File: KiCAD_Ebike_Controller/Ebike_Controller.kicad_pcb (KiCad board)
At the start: 4 copper layers, 100 x 100 mm, 118 parts, among them J1 IO, J10 I2C_SCL, J11 I2C_SDA, J2 Prog, J3 Hall Effect Sensors, J4 PHASE_A, J5 PHASE_B, J6 PHASE_C, J7 Micro_SD_Card, J8 +48V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

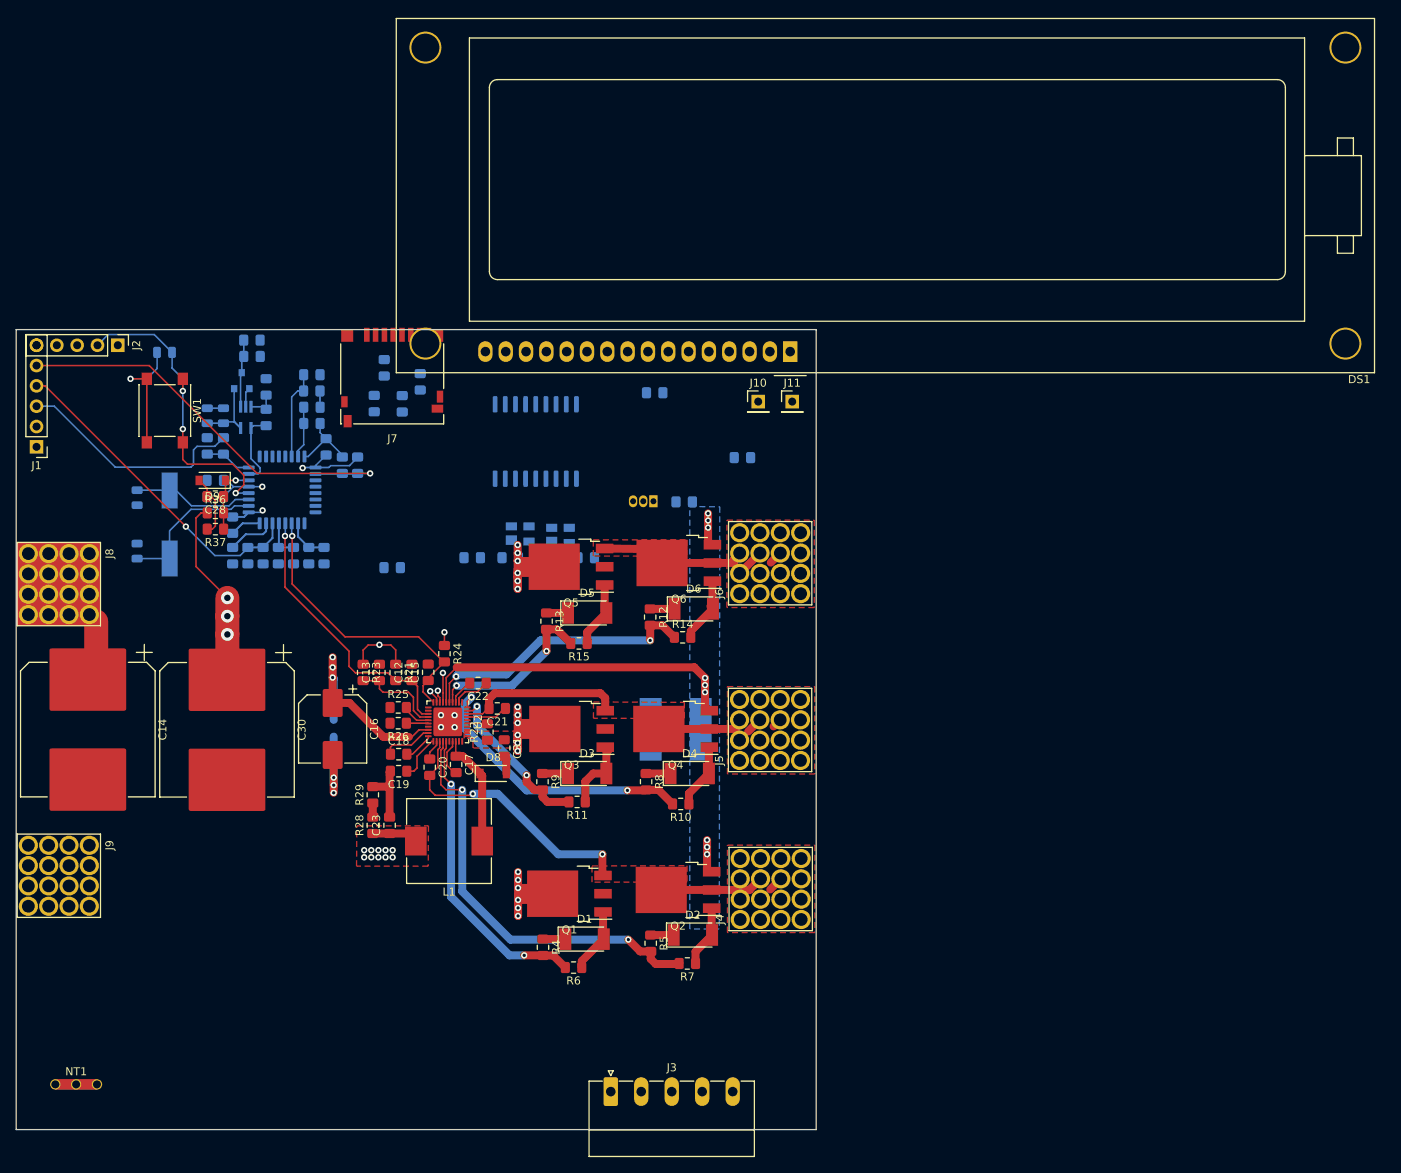
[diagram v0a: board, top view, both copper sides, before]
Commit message: Layout done. will tidy up ref des next
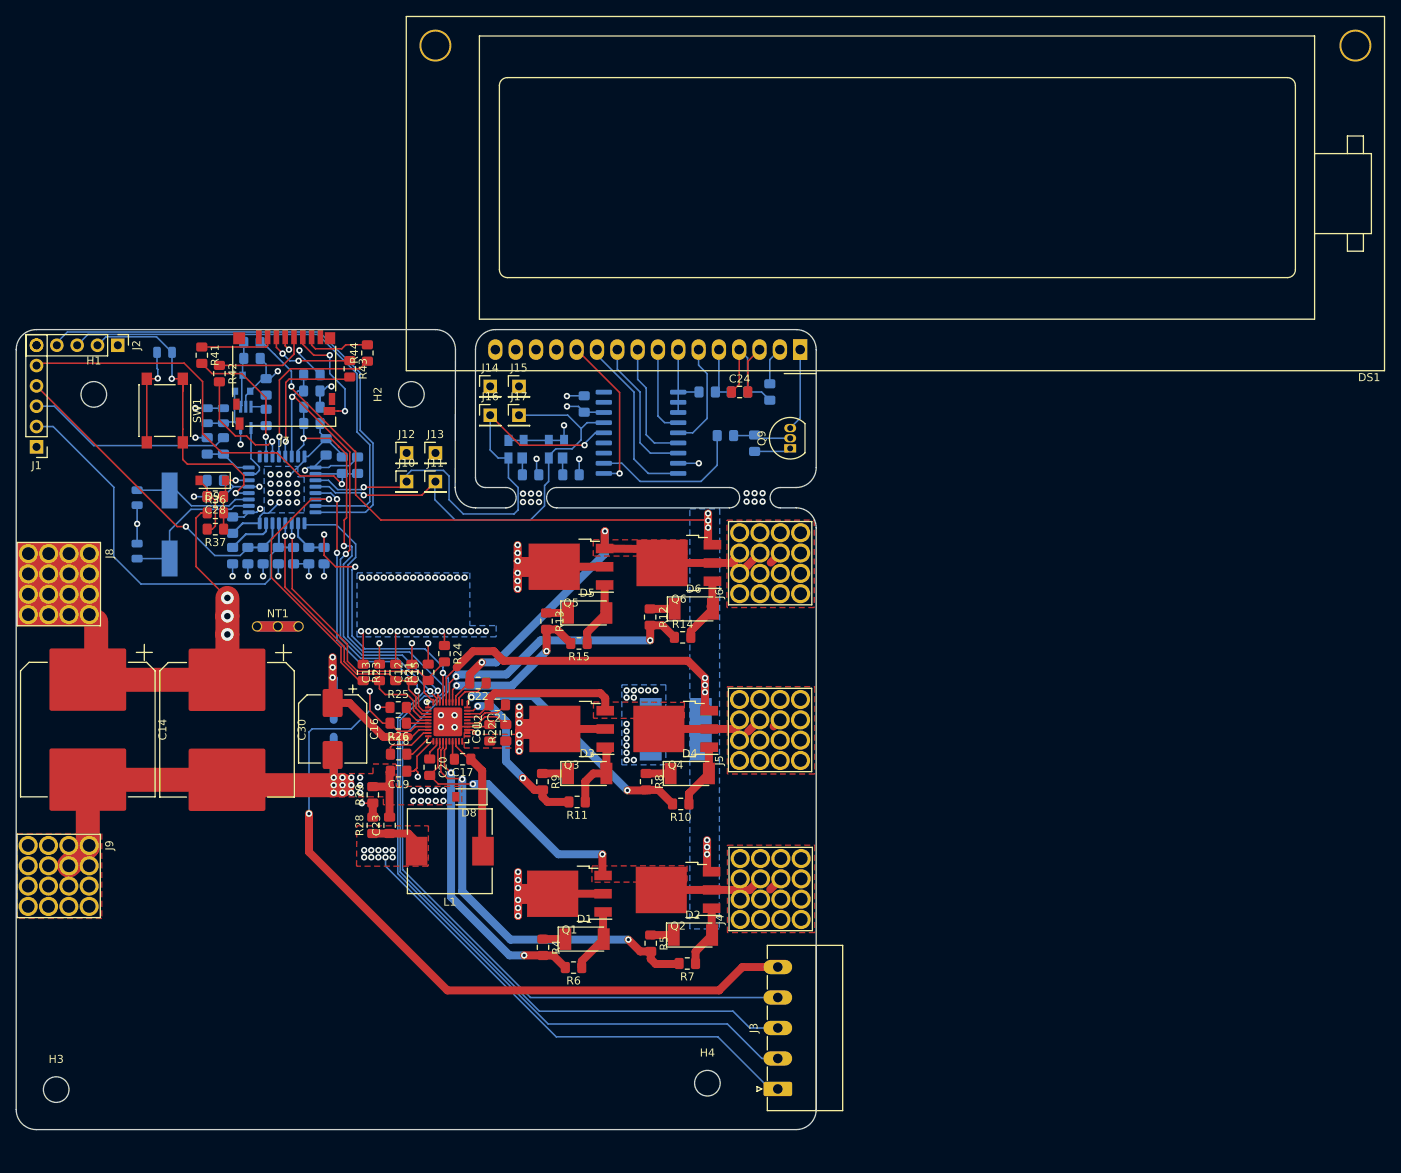
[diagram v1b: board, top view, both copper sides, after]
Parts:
- added H1: MountingHole, MountingHole:MountingHole_3.2mm_M3, F.Cu at (57.7, 67.1)
- added H2: MountingHole, MountingHole:MountingHole_3.2mm_M3, F.Cu at (97.4, 67.1)
- added H3: MountingHole, MountingHole:MountingHole_3.2mm_M3_DIN965, F.Cu at (53.0, 154.0)
- added H4: MountingHole, MountingHole:MountingHole_3.2mm_M3_DIN965, F.Cu at (134.4, 153.2)
- added J12: +3V3, Connector_PinHeader_2.54mm:PinHeader_1x01_P2.54mm_Vertical, F.Cu at (96.8, 74.4)
- added J13: GNDD, Connector_PinHeader_2.54mm:PinHeader_1x01_P2.54mm_Vertical, F.Cu at (100.4, 74.4)
- added J14: +3V3_S, Connector_PinHeader_2.54mm:PinHeader_1x01_P2.54mm_Vertical, F.Cu at (107.2, 66.1)
- added J15: GNDD_S, Connector_PinHeader_2.54mm:PinHeader_1x01_P2.54mm_Vertical, F.Cu at (110.8, 66.1)
- added J16: I2C_SCL_S, Connector_PinHeader_2.54mm:PinHeader_1x01_P2.54mm_Vertical, F.Cu at (107.2, 69.7)
- added J17: I2C_SDA_S, Connector_PinHeader_2.54mm:PinHeader_1x01_P2.54mm_Vertical, F.Cu at (110.8, 69.7)
- C24, Q9, R41, R42, R43, R44: moved to F.Cu
- moved NT1 62.6 mm to (78.1, 96.1)
- moved C24 48.7 mm to (138.4, 66.8)
- moved J11 45.7 mm to (100.4, 78.0)
- moved J10 45.1 mm to (96.8, 78.0)
- moved R20 33.7 mm to (140.3, 73.2), turned to 270 degrees
- moved R32 28.2 mm to (138.4, 66.8), turned to 180 degrees
- moved R30 26.6 mm to (112.3, 77.2)
- moved C25 23.8 mm to (119.0, 68.3), turned to 90 degrees
- moved R42 23.2 mm to (73.4, 64.5)
- moved R41 22.4 mm to (71.2, 62.2)
- moved J3 20.9 mm to (143.2, 153.9), turned to 90 degrees
- moved Q9 18.3 mm to (144.8, 73.8), turned to 90 degrees
- moved R35 17.2 mm to (136.7, 72.2), turned to 180 degrees
- moved R34 14.4 mm to (142.2, 66.8), turned to 90 degrees
- moved R33 14.0 mm to (134.4, 66.8)
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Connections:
- J10 pad 1: /LCD/LCD_I2C_1 -> /LCD/LCD_I2C1
- J11 pad 1: /LCD/LCD_I2C_2 -> /LCD/LCD_I2C2
- Q7 pad 2: /LCD/LCD_I2C_1 -> /LCD/LCD_I2C1
- Q8 pad 2: /LCD/LCD_I2C_2 -> /LCD/LCD_I2C2
- R41 pad 2: /SD CARD/SD_SPI_1 -> /MCU/SD_SPI1
- R42 pad 2: /SD CARD/SD_SPI_2 -> /MCU/SD_SPI2
- R43 pad 2: /SD CARD/SD_SPI_4 -> /MCU/SD_SPI4
- R44 pad 1: /SD CARD/SD_SPI_3 -> /MCU/SD_SPI3
- U1 pad 10: /MCU/SD_SPI_1 -> /MCU/SD_SPI1
- U1 pad 11: /MCU/SD_SPI_2 -> /MCU/SD_SPI2
- U1 pad 12: /MCU/SD_SPI_3 -> /MCU/SD_SPI3
- U1 pad 13: /MCU/SD_SPI_4 -> /MCU/SD_SPI4
- U1 pad 19: /MCU/LCD_I2C_1 -> /LCD/LCD_I2C1
- U1 pad 20: /MCU/LCD_I2C_2 -> /LCD/LCD_I2C2
- U2 pad 34: GNDD -> GND
- U3 pad 14: /LCD/LCD_I2C_1 -> /LCD/LCD_I2C1
- U3 pad 15: /LCD/LCD_I2C_2 -> /LCD/LCD_I2C2
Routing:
- net GNDD: track 0.00 -> 166.4 mm, vias 0 -> 11
- net /BLDC Driver/HA: track 13.0 -> 142.7 mm, vias 1 -> 3
- net /MCU/HALL_B_PB1: track 8.01 -> 134.1 mm, vias 1 -> 3
- net /MCU/HALL_C_PB3: track 9.16 -> 121.1 mm, vias 1 -> 3
- net /+3.3V: track 48.2 -> 149.7 mm, vias 15 -> 54
- net /LSS: track 50.3 -> 121.5 mm, vias 9 -> 10
- net /SWCLK: track 0.00 -> 65.7 mm
- net /LCD/LCD_I2C1: track 0.00 -> 62.0 mm, vias 0 -> 2
- net /SWDIO: track 0.00 -> 61.2 mm
- net /LCD/LCD_I2C2: track 0.00 -> 58.3 mm, vias 0 -> 1
- net GND: track 21.0 -> 76.9 mm, vias 7 -> 40
- net /BRAKE_SW_BP6: track 4.95 -> 52.0 mm
- net GNDA: track 41.2 -> 80.8 mm, vias 1 -> 25
- net /BLDC Driver/PWM_PA0: track 0.00 -> 38.2 mm, vias 0 -> 1
- net /BLDC Driver/DIR_PA1: track 0.00 -> 37.2 mm, vias 0 -> 3
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- added copper zone on B.Cu, net /+3.3V
- added copper zone on B.Cu, net GND
- added copper zone on F.Cu, net GND
- added copper zone on B.Cu, net GNDA
- added copper zone on In2.Cu, net GNDA
- added copper zone on In2.Cu, net GNDD
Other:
- outline, holes or cut-outs redrawn

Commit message: Finished ready for fab
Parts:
- added RT1: R_Thermal, Resistor_SMD:R_1206_3216Metric_Pad1.42x1.75mm_HandSolder, F.Cu at (114.3, 104.1)
- added RT2: R_Thermal, Resistor_SMD:R_1206_3216Metric_Pad1.42x1.75mm_HandSolder, F.Cu at (129.3, 124.4)
- added RT3: R_Thermal, Resistor_SMD:R_1206_3216Metric_Pad1.42x1.75mm_HandSolder, F.Cu at (116.1, 124.7)
- added RT4: R_Thermal, Resistor_SMD:R_1206_3216Metric_Pad1.42x1.75mm_HandSolder, F.Cu at (130.5, 102.9)
- added RT5: R_Thermal, Resistor_SMD:R_1206_3216Metric_Pad1.42x1.75mm_HandSolder, F.Cu at (116.4, 84.0)
- added RT6: R_Thermal, Resistor_SMD:R_1206_3216Metric_Pad1.42x1.75mm_HandSolder, F.Cu at (128.7, 83.7)
- Star GND: renamed from NT1
- moved Q6 0.33 mm to (130.8, 88.5)
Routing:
- net GNDD: track 166.4 -> 217.2 mm, vias 11 -> 15
- net +48V: track 153.3 -> 170.4 mm
- net /Triple_H_Bridge/PHASE_B: track 35.5 -> 38.1 mm
- net /LSS: track 121.5 -> 123.3 mm, vias 10 -> 11
- net /MODE1_SW_PB7: track 41.1 -> 42.4 mm
- net GND: vias 40 -> 76
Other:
- board text added: "+"
- board text added: "-"
- board text added: "BATT +"
- board text added: "BATT -"
- board text added: "Hall A"
- board text added: "Hall B"
- board text added: "Hall C"
- board text added: "for Maijki"

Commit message: done and gerbes sent to JLC
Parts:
- added D11: STPS2L60ZFY, Diode_SMD:D_SOD-123, B.Cu at (64.3, 68.2)
- added D12: STPS2L60ZFY, Diode_SMD:D_SOD-123, F.Cu at (56.8, 80.9)
- added D13: STPS2L60ZFY, Diode_SMD:D_SOD-123, F.Cu at (60.6, 79.2)
- added SW2: SW_SPST, Connector_PinHeader_2.54mm:PinHeader_1x02_P2.54mm_Vertical, F.Cu at (50.5, 78.4)
- NT1: renamed from Star GND
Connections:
- C13 pad 1: /MCU/nSLEEP_PA12 -> /BLDC Driver/nSLEEP_PA12
- J2 pad 1: /+3.3V -> Net-(D11-Pad2)
- R23 pad 2: /MCU/nSLEEP_PA12 -> /BLDC Driver/nSLEEP_PA12
- U2 pad 14: /MCU/nSLEEP_PA12 -> /BLDC Driver/nSLEEP_PA12
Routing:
- net /BLDC Driver/nSLEEP_PA12: track 0.00 -> 59.2 mm, vias 0 -> 2
- net /BMS/V_BATT_MON_PA0: track 9.11 -> 36.4 mm, vias 1 -> 3
- net /+3.3V: track 149.7 -> 157.7 mm
- net Net-(D11-Pad2): track 0.00 -> 7.09 mm
- net Net-(D12-Pad2): track 0.00 -> 4.62 mm
- net GNDA: track 80.8 -> 82.4 mm
- net /MCU/nSLEEP_PA12: track 45.0 -> 44.1 mm, vias 1 -> 3
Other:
- board text added: "Phase A"
- board text added: "Phase B"
- board text added: "Phase C"
- board text added: "eBike Controller 48V @ 20A HW - V1.0 SW -"
- board text added: "eBike Speedo HW - V1.0 SW -"

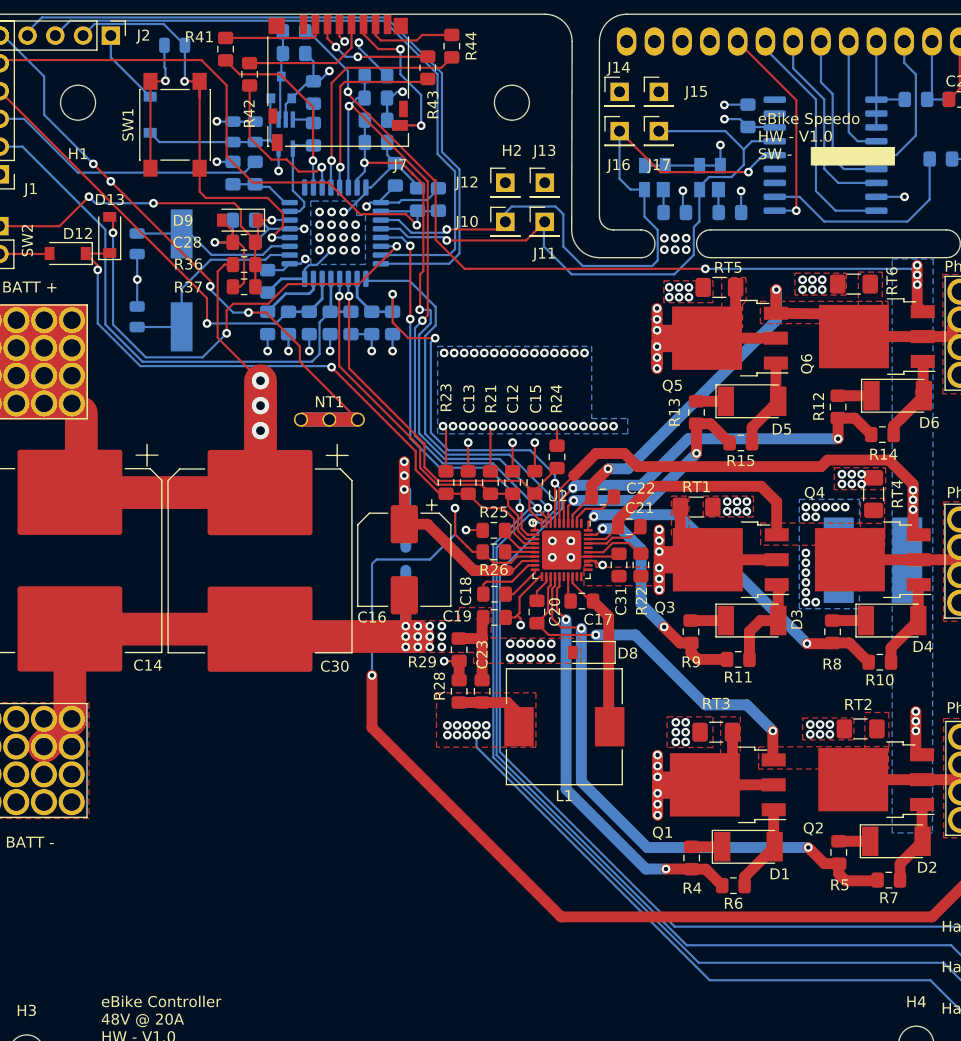
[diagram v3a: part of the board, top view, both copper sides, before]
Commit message: Added JLC serial number and my logo
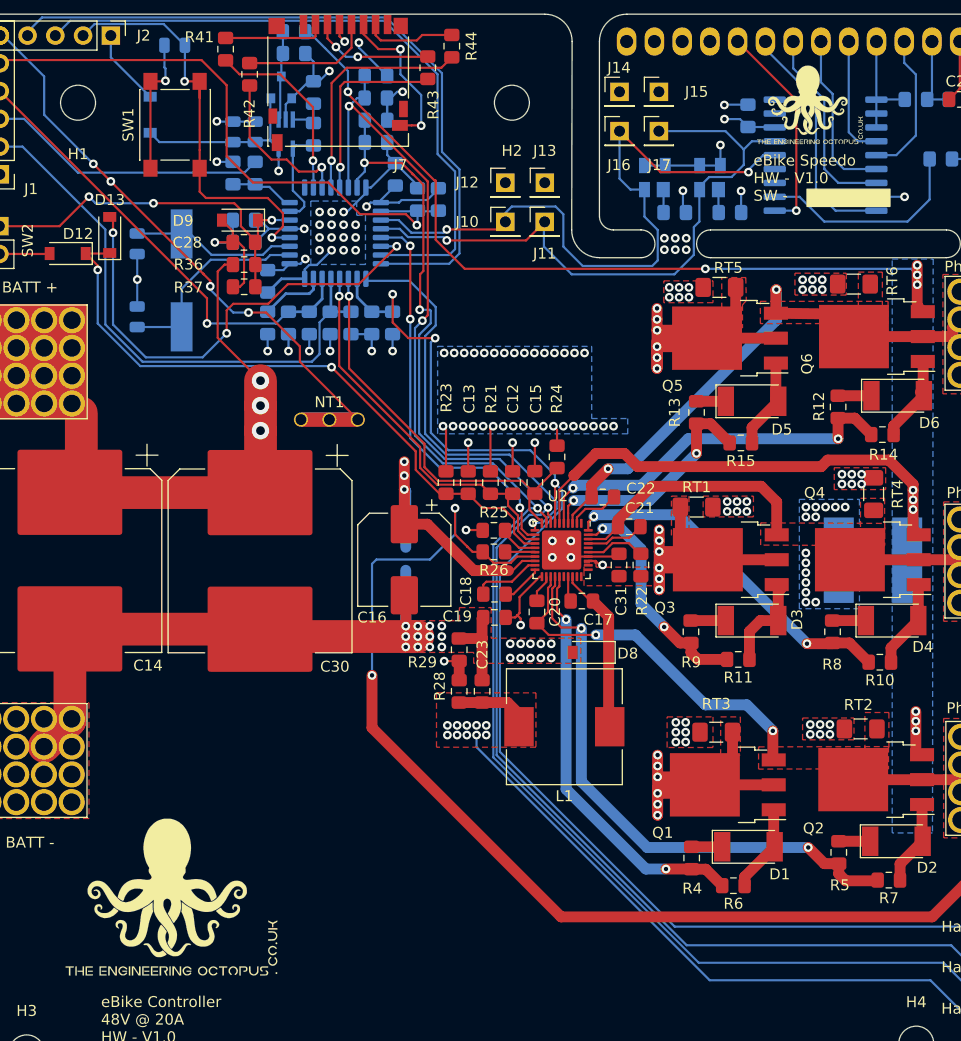
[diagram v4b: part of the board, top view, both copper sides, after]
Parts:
- added G***: LOGO, otk:newlogo, F.Cu at (124.7, 67.3)
- added G***: LOGO, otk:logo_big, F.Cu at (66.3, 139.8)
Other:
- board text added: "JLCJLCJLCJLC"

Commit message: updating the repo
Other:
- board text added: "3893385"
- board text removed: "for Maijki"
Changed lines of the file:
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@@
   (general
     (thickness 1.6)
-    (drawings 45)
+    (drawings 66)
     (tracks 1266)
     (zones 0)
@@
   (layers
     (0 F.Cu signal)
-    (1 In1.Cu power hide)
-    (2 In2.Cu power hide)
+    (1 In1.Cu power)
+    (2 In2.Cu power)
     (31 B.Cu signal)
-    (32 B.Adhes user hide)
-    (33 F.Adhes user hide)
-    (34 B.Paste user hide)
+    (32 B.Adhes user)
+    (33 F.Adhes user)
+    (34 B.Paste user)
     (35 F.Paste user)
     (36 B.SilkS user)
     (37 F.SilkS user)
-    (38 B.Mask user hide)
-    (39 F.Mask user hide)
-    (40 Dwgs.User user hide)
-    (41 Cmts.User user hide)
-    (42 Eco1.User user hide)
-    (43 Eco2.User user hide)
+    (38 B.Mask user)
+    (39 F.Mask user)
+    (40 Dwgs.User user)
+    (41 Cmts.User user)
+    (42 Eco1.User user)
+    (43 Eco2.User user)
     (44 Edge.Cuts user)
-    (45 Margin user hide)
+    (45 Margin user)
     (46 B.CrtYd user)
     (47 F.CrtYd user)
-    (48 B.Fab user hide)
-    (49 F.Fab user hide)
+    (48 B.Fab user)
+    (49 F.Fab user)
   )
   (setup
@@
     )
   )
-  (module Package_SO:SOIC-18W_7.5x11.6mm_P1.27mm (layer B.Cu)
+  (module Package_SO:SOIC-18W_7.5x11.6mm_P1.27mm locked (layer B.Cu)
     (at 126.1 71.9 180)
     (descr "SOIC, 18 Pin (JEDEC MS-013AB, https://www.analog.com/media/en/package-pcb-resources/package/33254132129439rw_18.pdf), generated with kicad-footprint-generator ipc_gullwing_generator.py")
@@
     )
   )
-  (module Package_QFP:LQFP-32_7x7mm_P0.8mm locked (layer B.Cu)
+  (module Package_QFP:LQFP-32_7x7mm_P0.8mm (layer B.Cu)
     (at 81.2378 79.0376)
     (descr "LQFP, 32 Pin (https://www.nxp.com/docs/en/package-information/SOT358-1.pdf), generated with kicad-footprint-generator ipc_gullwing_generator.py")
@@
     )
   )
+  (gr_poly (pts (xy 52.45 105.15) (xy 52.45 104.35) (xy 52.15 104.35) (xy 52.15 105.15)) (layer B.SilkS) (width 0.1))
+  (gr_poly (pts (xy 54.35 105.45) (xy 54.35 103.95) (xy 54.25 103.95) (xy 54.25 105.45)) (layer B.SilkS) (width 0.1))
+  (gr_poly (pts (xy 53.6 105.05) (xy 53.6 103.95) (xy 53.5 103.95) (xy 53.5 105.05)) (layer B.SilkS) (width 0.1))
+  (gr_poly (pts (xy 52.85 105.45) (xy 52.85 103.95) (xy 52.75 103.95) (xy 52.75 105.45)) (layer B.SilkS) (width 0.1))
+  (gr_line (start 52.35 104.35) (end 52.25 104.35) (layer B.SilkS) (width 0.12))
+  (gr_line (start 52.45 104.35) (end 52.35 104.35) (layer B.SilkS) (width 0.12))
+  (gr_line (start 52.45 105.15) (end 52.45 104.35) (layer B.SilkS) (width 0.12))
+  (gr_line (start 52.35 105.15) (end 52.45 105.15) (layer B.SilkS) (width 0.12))
+  (gr_line (start 52.15 105.15) (end 52.25 105.15) (layer B.SilkS) (width 0.12))
+  (gr_line (start 52.15 104.35) (end 52.15 105.15) (layer B.SilkS) (width 0.12))
+  (gr_line (start 52.25 104.35) (end 52.15 104.35) (layer B.SilkS) (width 0.12))
+  (gr_line (start 54.85 103.48) (end 52.31 103.48) (layer B.SilkS) (width 0.12))
+  (gr_line (start 54.85 106.02) (end 54.85 103.48) (layer B.SilkS) (width 0.12))
+  (gr_line (start 52.31 106.02) (end 54.85 106.02) (layer B.SilkS) (width 0.12))
+  (gr_line (start 52.31 103.48) (end 52.31 106.02) (layer B.SilkS) (width 0.12))
+  (gr_arc (start 55.25 102.85) (end 55.25 101.75) (angle 90) (layer B.SilkS) (width 0.12))
+  (gr_arc (start 51.65 102.85) (end 50.55 102.85) (angle 90) (layer B.SilkS) (width 0.12))
+  (gr_line (start 51.65 101.75) (end 55.25 101.75) (layer B.SilkS) (width 0.12))
+  (gr_line (start 55.25 115.35) (end 51.65 115.35) (layer B.SilkS) (width 0.12))
+  (gr_arc (start 51.65 114.25) (end 51.65 115.35) (angle 90) (layer B.SilkS) (width 0.12))
+  (gr_arc (start 55.25 114.25) (end 56.35 114.25) (angle 90) (layer B.SilkS) (width 0.12))
+  (gr_text 3893385 (at 53.6 110.55 90) (layer B.SilkS)
+    (effects (font (size 1 1) (thickness 0.15)) (justify mirror))
+  )
   (gr_text JLCJLCJLCJLC (at 140.4 77.4) (layer B.SilkS)
     (effects (font (size 1 1) (thickness 0.153)) (justify mirror))
@@
     (effects (font (size 1 1) (thickness 0.15)) (justify left))
   )
-  (gr_text "for Maijki" (at 97.4 153) (layer In1.Cu)
-    (effects (font (size 5 5) (thickness 1)))
-  )
   (gr_text + (at 139.4 153.8) (layer F.SilkS)
